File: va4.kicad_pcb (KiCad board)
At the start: 2 copper layers, 95.8 x 73.1 mm, 19 parts, among them J1 LED, J2 MJ-4PP-9, SW1 RESET_SWITCH, SW2 SW_PUSH, SW3 SW_PUSH, SW4 SW_PUSH, SW5 SW_PUSH, U1 ProMicro

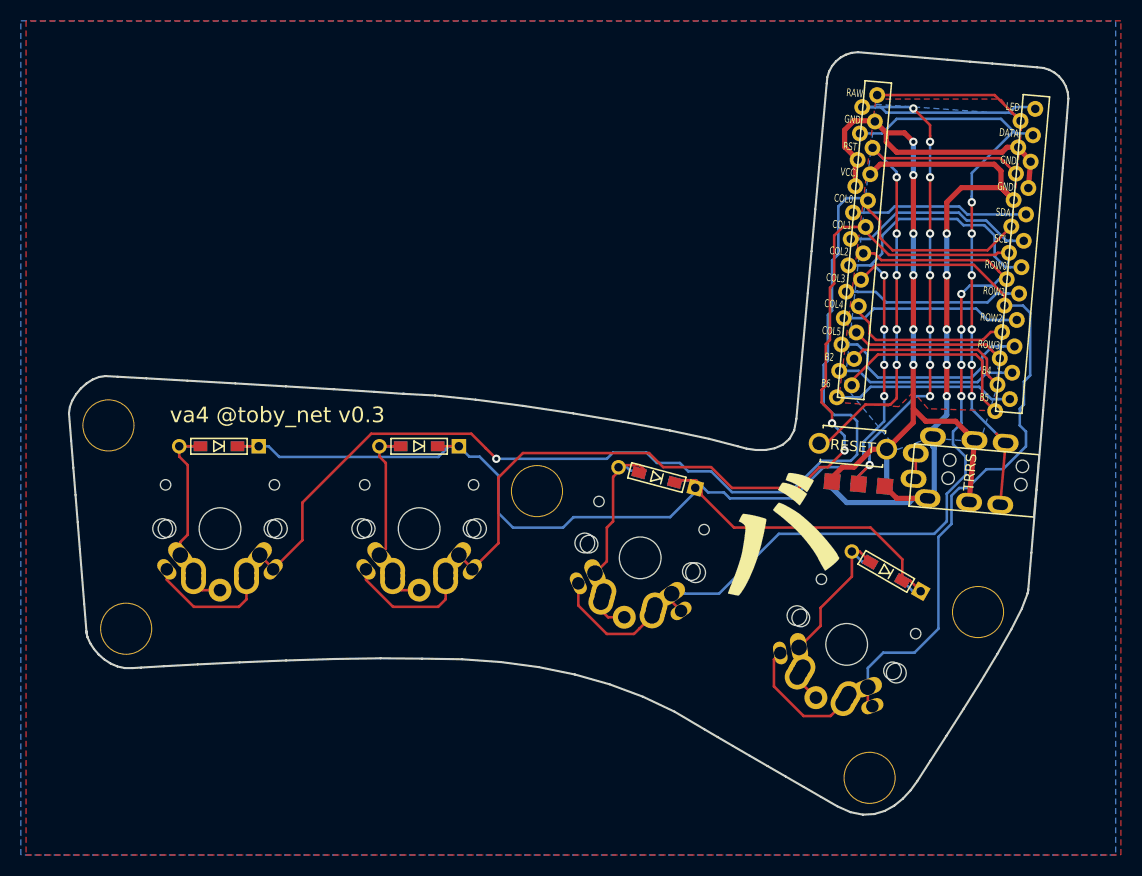
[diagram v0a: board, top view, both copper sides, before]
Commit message: Rotary encoder with mx SW5
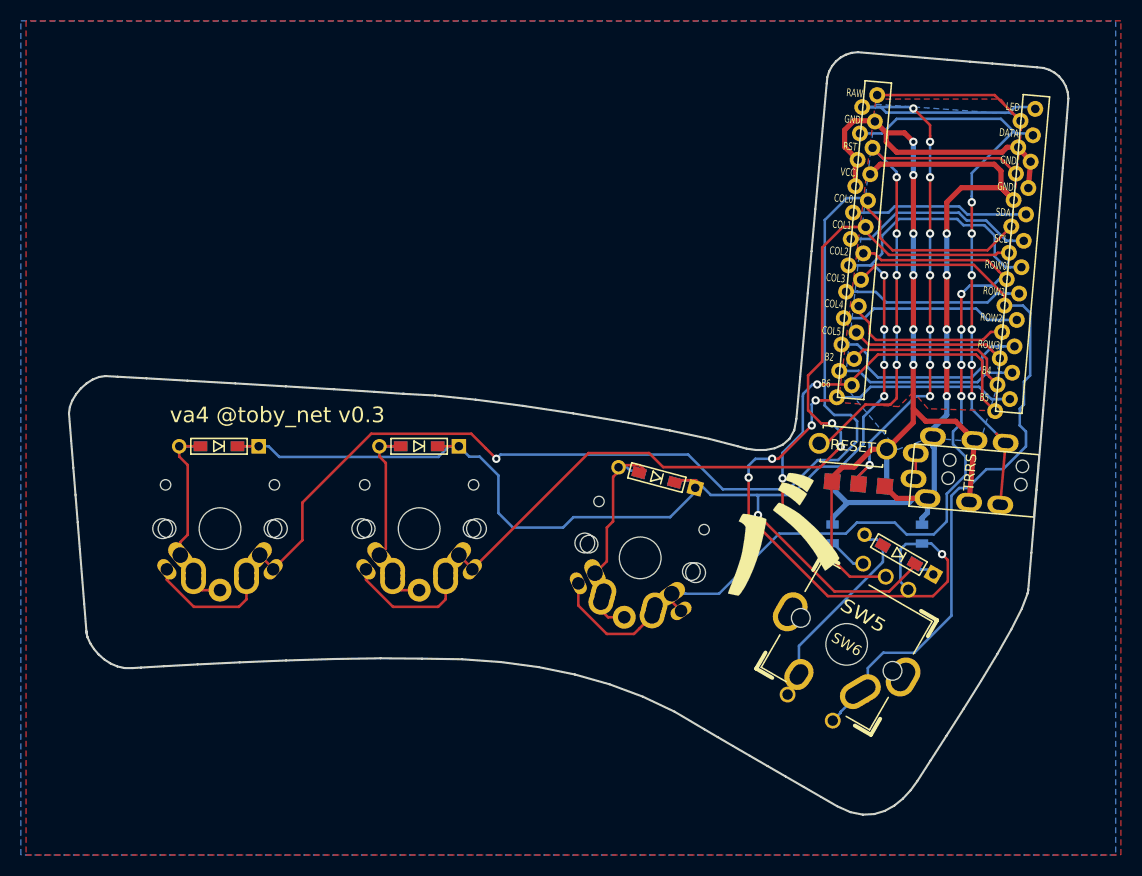
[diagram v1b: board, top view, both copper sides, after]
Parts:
- removed Ref** (x5): Val**, kbd:HOLE
- added R1: 5k, Resistors:0805, B.Cu at (123.4, 74.2)
- added R2: 5k, Resistors:0805, B.Cu at (114.8, 74.2)
- added SW6: Rotary_Encoder_Switch, AcheronHardware:ALPS_EC11E, F.Cu at (116.2, 84.8)
- SW5: footprint kbd:MX_ALPS_PG1350_noLed -> Keebio-Parts:Hybrid_PCB_100H
- moved D4 2.02 mm to (121.2, 76.2)
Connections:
- net Net-(D4-Pad2) renamed Enc1Row0
- U1 pad 12: Net-(U1-Pad12) -> encA
- U1 pad 13: Net-(U1-Pad13) -> encB
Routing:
- net encA: track 0.00 -> 69.1 mm, vias 0 -> 5
- net encB: track 0.00 -> 46.5 mm, vias 0 -> 3
- net Net-(U1-Pad13): track 19.6 -> 0.00 mm
- net Net-(U1-Pad12): track 17.5 -> 0.00 mm
- net GND: track 86.3 -> 99.6 mm
- net col3: track 80.6 -> 72.1 mm
- net row0: track 152.2 -> 144.9 mm, vias 4 -> 5
- net VCC: track 68.9 -> 74.3 mm
- net col1: track 103.1 -> 98.7 mm
- net col0: track 133.1 -> 130.2 mm
- net col2: track 87.5 -> 88.4 mm

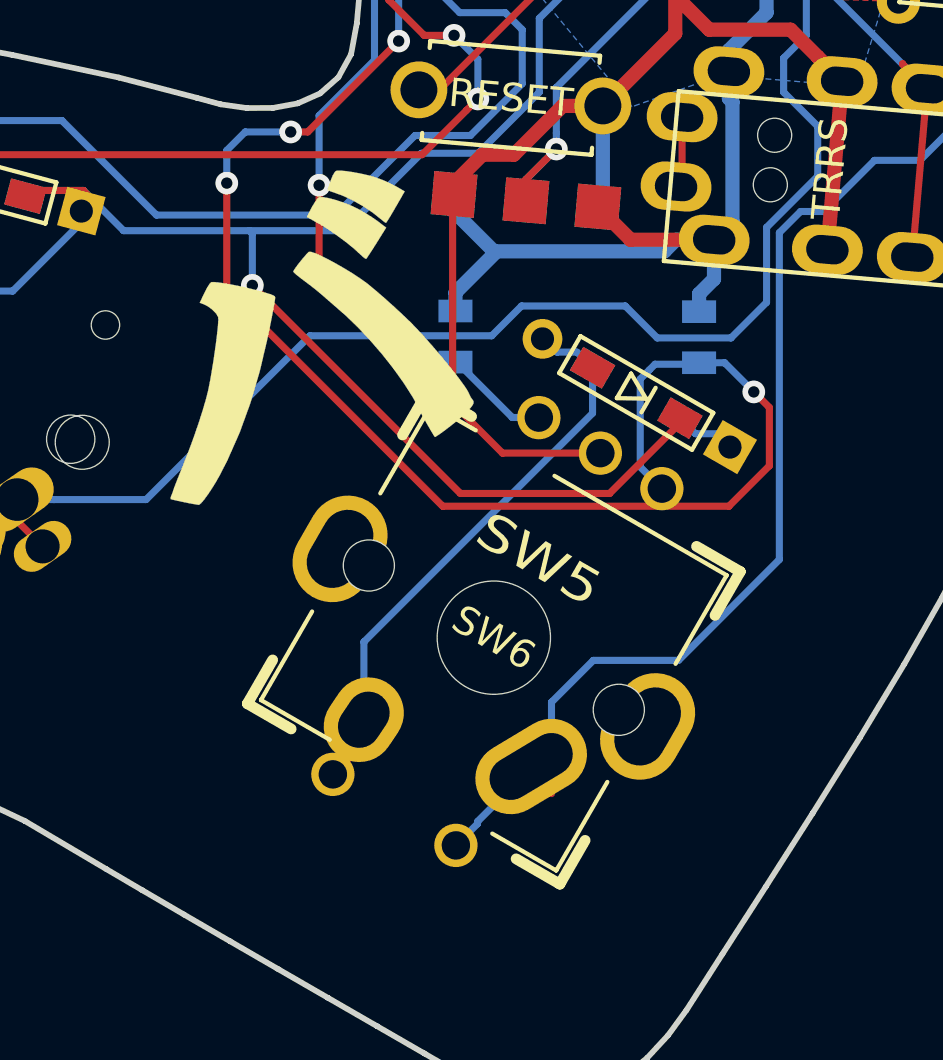
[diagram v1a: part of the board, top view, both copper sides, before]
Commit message: choc mx hybrid with rotary encoder on SW5
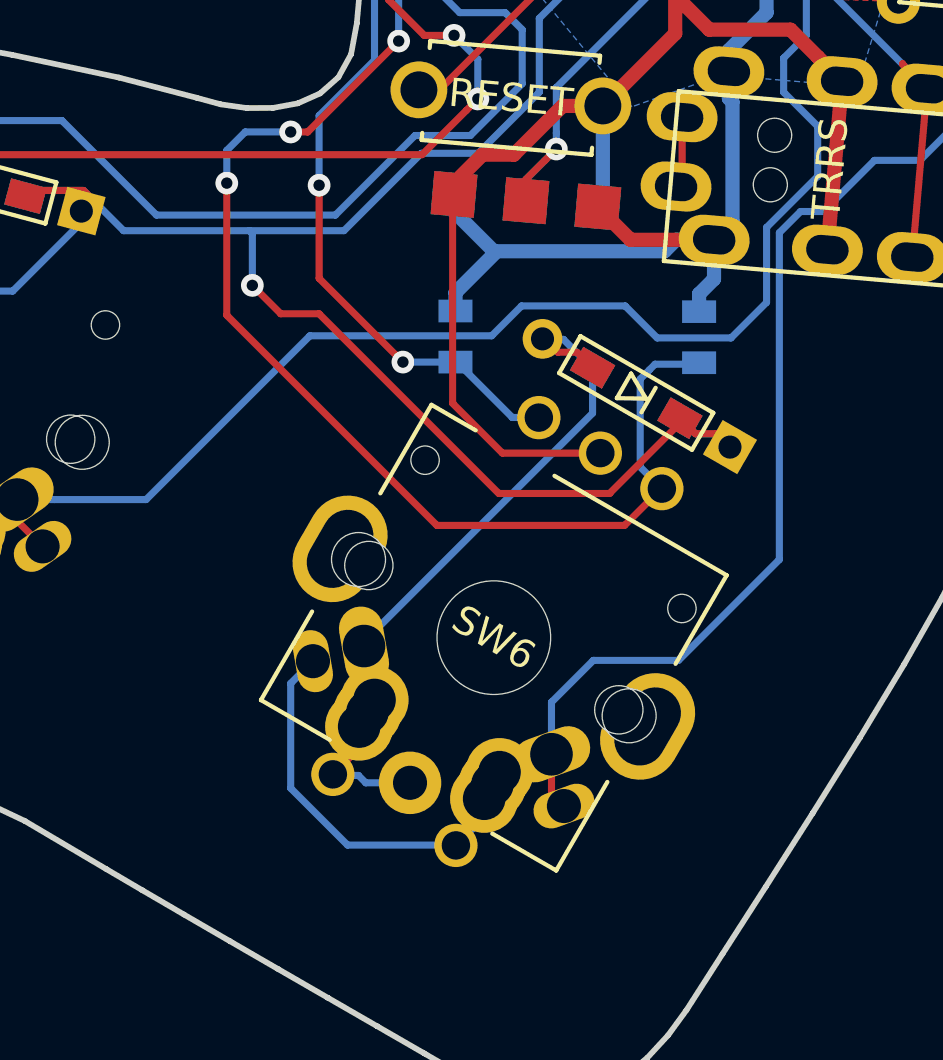
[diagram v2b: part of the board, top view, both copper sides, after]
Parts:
- removed G*** (x2): LOGO, my:logo-va_13.5mm
- SW5: footprint Keebio-Parts:Hybrid_PCB_100H -> kbd:MX_ALPS_PG1350_noLed
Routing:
- net col3: track 72.1 -> 83.6 mm
- net encA: track 69.1 -> 60.9 mm, vias 5 -> 4
- net Enc1Row0: track 20.3 -> 25.2 mm
- net row0: track 144.9 -> 147.1 mm

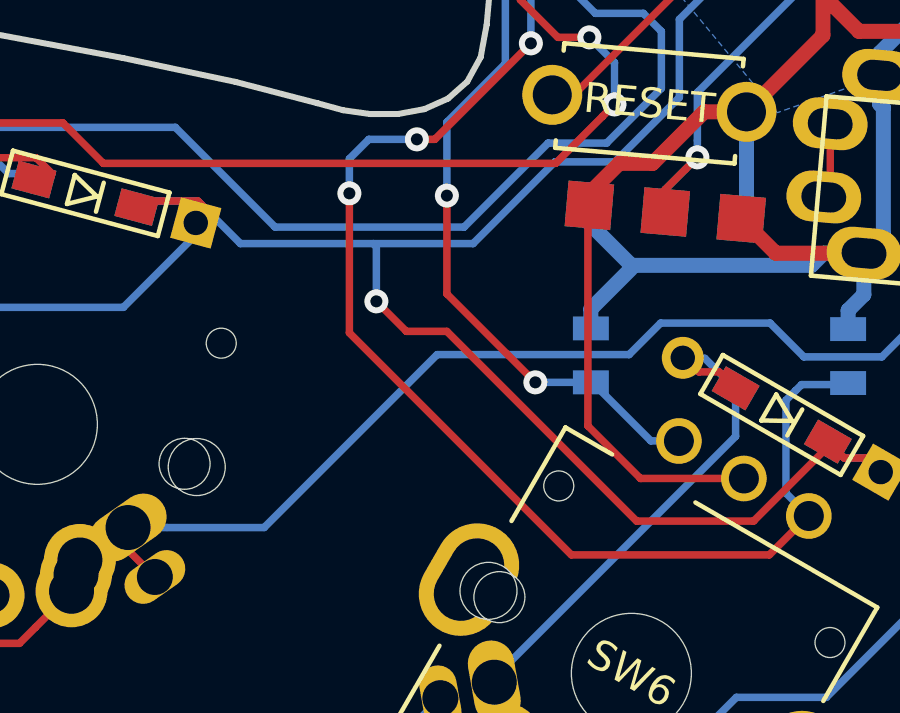
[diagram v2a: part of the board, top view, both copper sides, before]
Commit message: Add logos back in
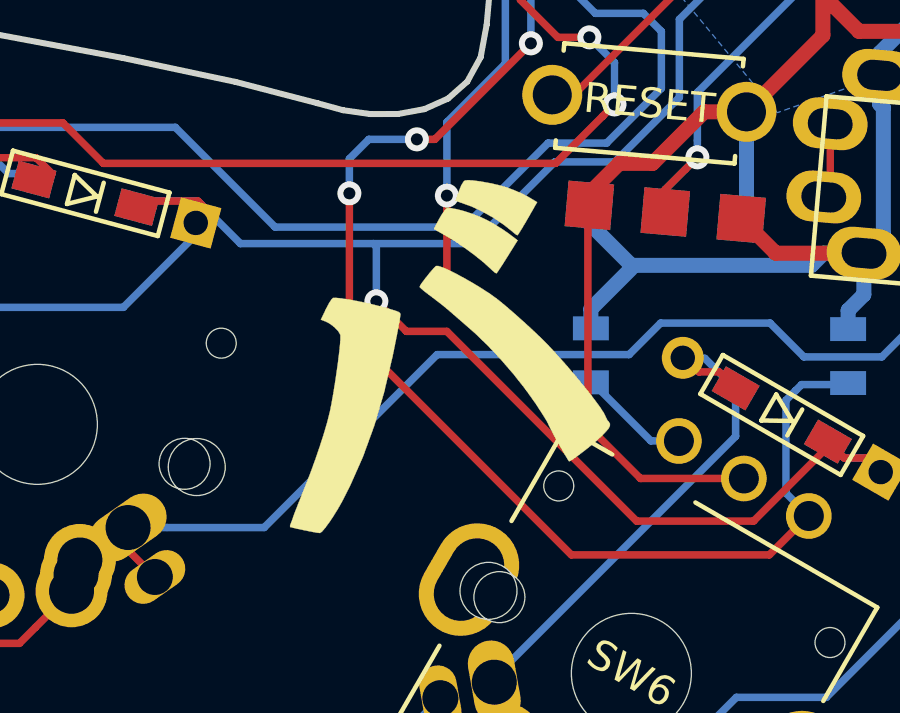
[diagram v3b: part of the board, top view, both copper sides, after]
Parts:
- added G***: LOGO, my:logo-va_13.5mm, B.Cu at (112.0, 74.4)
- added G***: LOGO, my:logo-va_13.5mm, F.Cu at (109.2, 74.4)
